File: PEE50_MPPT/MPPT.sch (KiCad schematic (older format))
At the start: 11 parts, among them J5 PV_IN1, Q1 BC547, U4 NTA4151PT1G

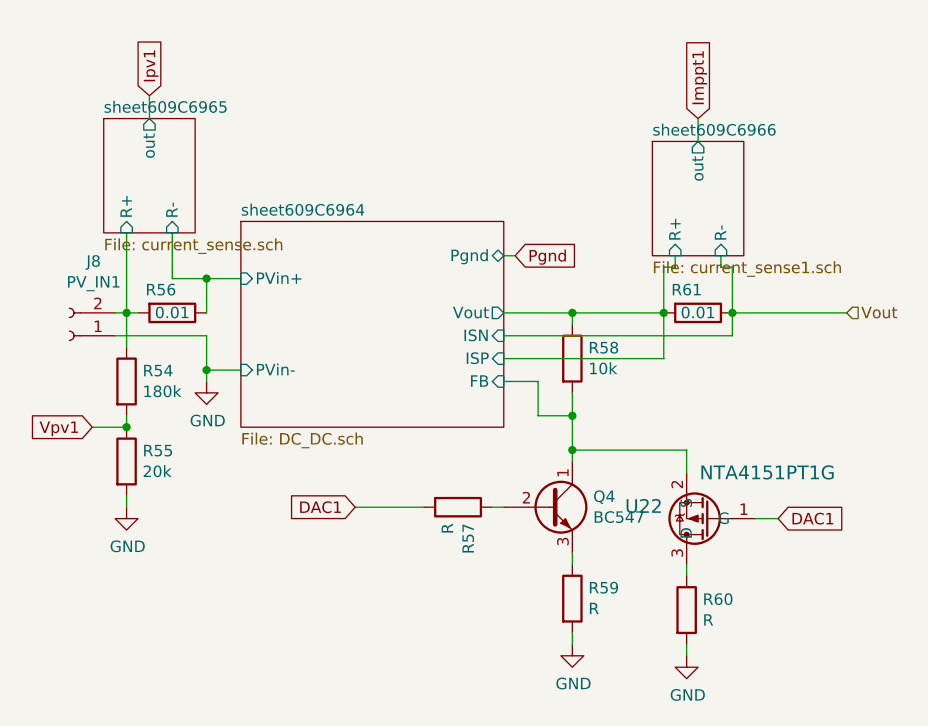
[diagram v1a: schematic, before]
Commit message: spinneweb aangemaakt
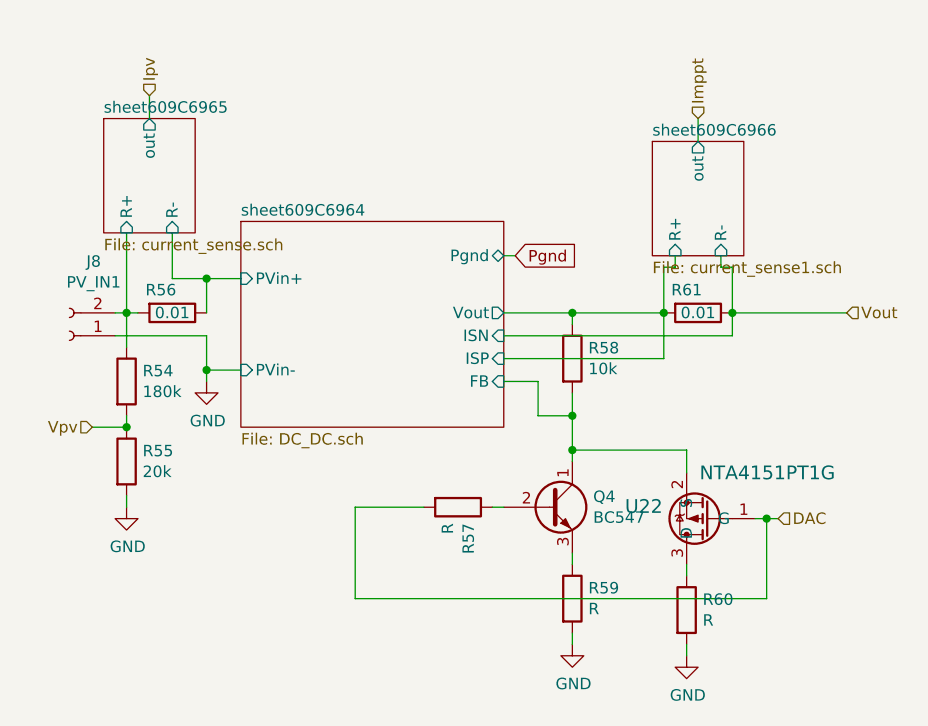
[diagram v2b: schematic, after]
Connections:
- net DAC1 renamed DAC
- net Vpv1 renamed Vpv
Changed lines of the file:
@@
 Wire Wire Line
 	5800 4200 5850 4200
-Text GLabel 5200 4200 0    50   Input ~ 0
-DAC1
 Wire Wire Line
 	5200 4200 5500 4200
-Text GLabel 4050 3850 0    50   Input ~ 0
-Vpv1
 Wire Wire Line
 	6850 3350 7350 3350
@@
 	4050 3850 4200 3850
 Connection ~ 4200 3850
-Text GLabel 4300 2400 1    50   Input ~ 0
-Ipv1
 Wire Wire Line
 	4300 2400 4300 2500
-Text GLabel 6700 2500 1    50   Input ~ 0
-Imppt1
 Wire Wire Line
 	6700 2500 6700 2600
@@
 Wire Wire Line
 	6650 4500 6650 4450
-Text GLabel 7050 4250 2    50   Input ~ 0
-DAC1
 Wire Wire Line
-	7050 4250 6950 4250
+	7050 4250 7000 4250
 Text HLabel 7350 3350 2    50   Input ~ 0
 Vout
+Text HLabel 6700 2500 1    50   Input ~ 0
+Imppt
+Text HLabel 4300 2400 1    50   Input ~ 0
+Ipv
+Text HLabel 7050 4250 2    50   Input ~ 0
+DAC
+Wire Wire Line
+	7000 4250 7000 4600
+Wire Wire Line
+	7000 4600 5200 4600
+Wire Wire Line
+	5200 4600 5200 4200
+Connection ~ 7000 4250
+Wire Wire Line
+	7000 4250 6950 4250
+Text HLabel 4050 3850 0    50   Input ~ 0
+Vpv
 $EndSCHEMATC
